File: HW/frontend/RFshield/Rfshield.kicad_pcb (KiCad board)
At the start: 4 copper layers, 73 x 50.9 mm, 139 parts, among them P10 TXENABLE, P11 RXENABLE, P2 VAA, P26 GND, P27 GND, P29 GND, P38 CLKIN, P39 CLKOUT, Q1 MOSFET_P, T1 RX_BALUN, T2 TX_BALUN, U1 MAX2837, U2 MAX5864, U3 SI5351C, X1 GSG-XTAL4PIN

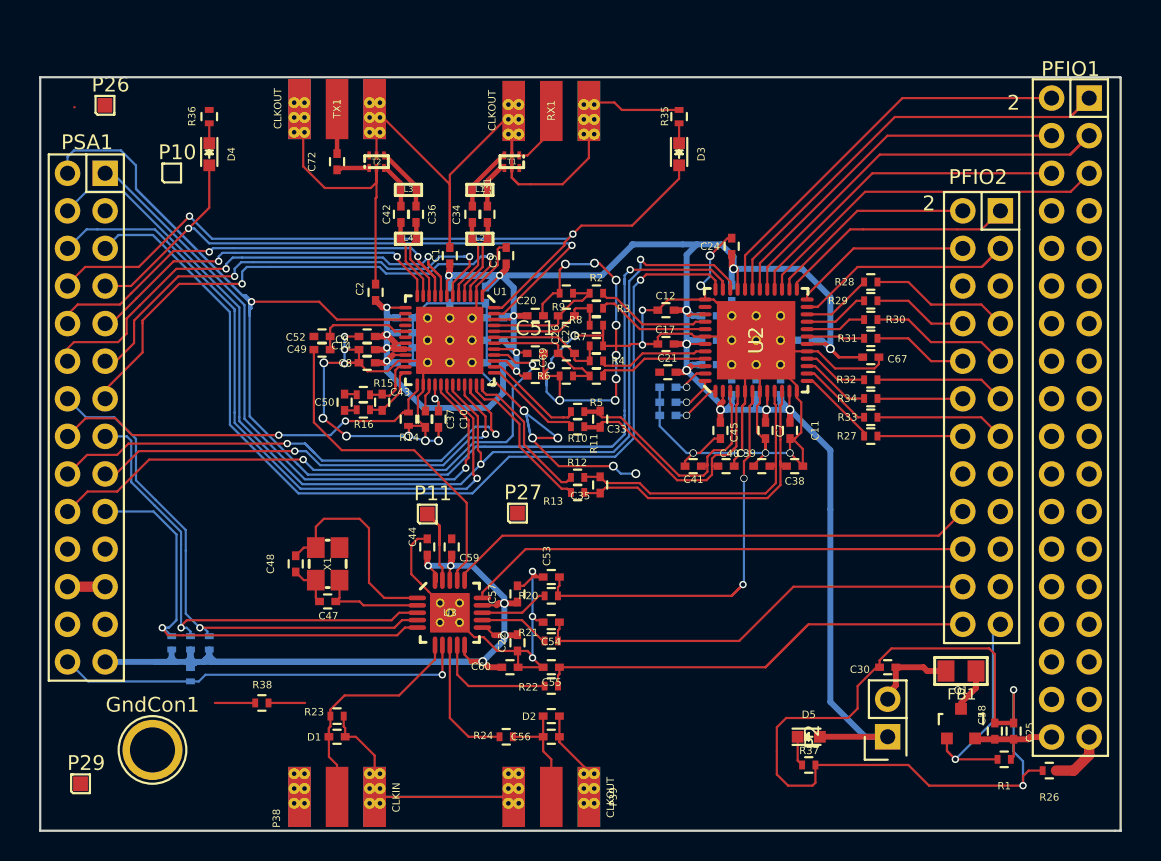
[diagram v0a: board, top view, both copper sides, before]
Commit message: bypass capacitors y planos de tierra agregados
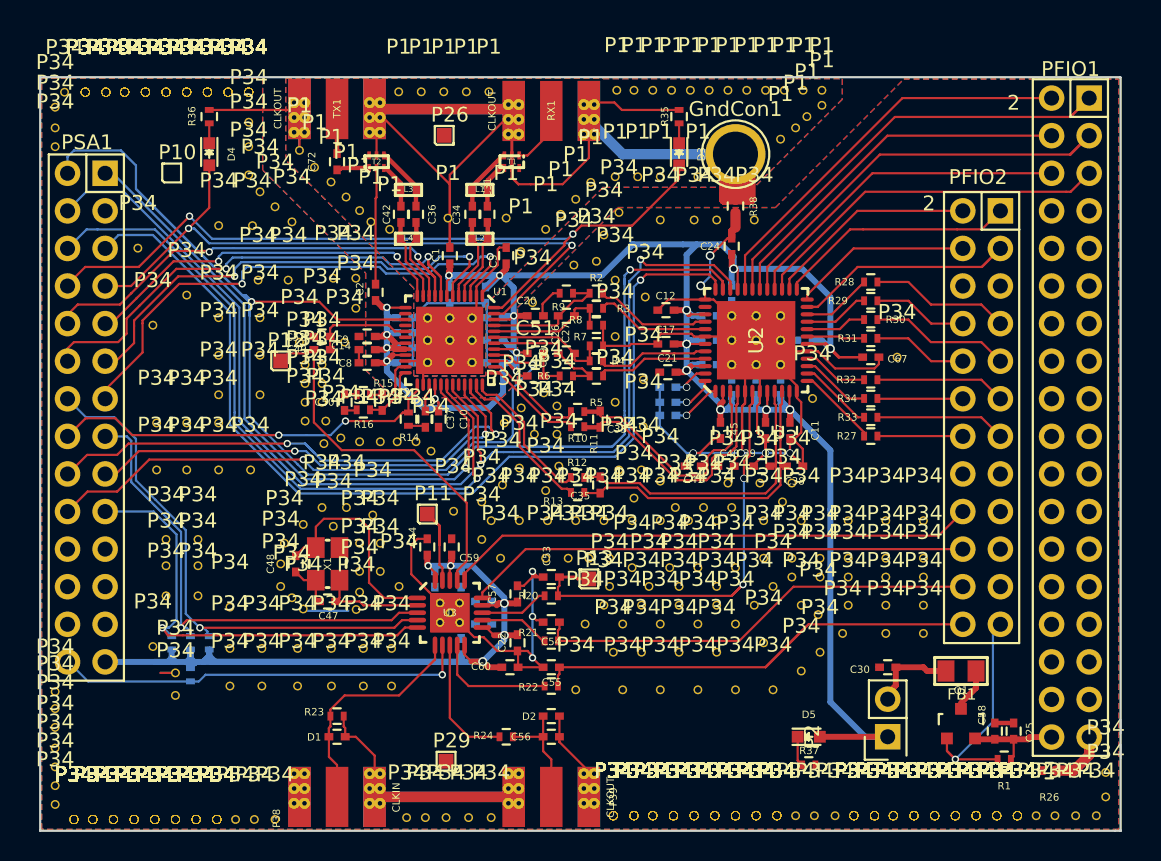
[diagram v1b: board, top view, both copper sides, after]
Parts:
- removed P27: GND, Connect:testpoint1mm
- added C70: 2.2uF, Capacitors_SMD:C_0402, B.Cu at (50.3, 104.1)
- added C71: 2.2uF, Capacitors_SMD:C_0402, B.Cu at (48.8, 105.7)
- added C73: 2.2uF, Capacitors_SMD:C_0402, B.Cu at (50.3, 102.6)
- added C74: 2.2uF, Capacitors_SMD:C_0402, B.Cu at (47.0, 101.1)
- added C75: 2.2uF, Capacitors_SMD:C_0402, B.Cu at (48.8, 101.1)
- added P1: CONN_01X01, Connect:GSG-HOLE-06mm1, F.Cu at (43.9, 77.5)
- added P1: CONN_01X01, Connect:GSG-HOLE-06mm1, F.Cu at (73.2, 69.1)
- added P1: CONN_01X01, Connect:GSG-HOLE-06mm1, F.Cu at (73.2, 68.1)
- added P1: CONN_01X01, Connect:GSG-HOLE-06mm1, F.Cu at (71.9, 68.1)
- added P1: CONN_01X01, Connect:GSG-HOLE-06mm1, F.Cu at (70.6, 68.1)
- added P1: CONN_01X01, Connect:GSG-HOLE-06mm1, F.Cu at (69.3, 68.1)
- added P1: CONN_01X01, Connect:GSG-HOLE-06mm1, F.Cu at (68.1, 68.1)
- added P1: CONN_01X01, Connect:GSG-HOLE-06mm1, F.Cu at (66.8, 68.1)
- added P1: CONN_01X01, Connect:GSG-HOLE-06mm1, F.Cu at (65.5, 68.1)
- added P1: CONN_01X01, Connect:GSG-HOLE-06mm1, F.Cu at (64.3, 68.1)
- added P1: CONN_01X01, Connect:GSG-HOLE-06mm1, F.Cu at (63.0, 68.1)
- added P1: CONN_01X01, Connect:GSG-HOLE-06mm1, F.Cu at (42.7, 77.0)
- added P1: CONN_01X01, Connect:GSG-HOLE-06mm1, F.Cu at (61.7, 68.1)
- added P1: CONN_01X01, Connect:GSG-HOLE-06mm1, F.Cu at (40.0, 74.3)
- added P1: CONN_01X01, Connect:GSG-HOLE-06mm1, F.Cu at (60.5, 68.1)
- added P1: CONN_01X01, Connect:GSG-HOLE-06mm1, F.Cu at (59.3, 68.1)
- added P1: CONN_01X01, Connect:GSG-HOLE-06mm1, F.Cu at (52.8, 79.0)
- added P1: CONN_01X01, Connect:GSG-HOLE-06mm1, F.Cu at (38.9, 73.3)
- added P1: CONN_01X01, Connect:GSG-HOLE-06mm1, F.Cu at (41.0, 75.3)
- added P1: CONN_01X01, Connect:GSG-HOLE-06mm1, F.Cu at (37.8, 72.1)
- added P1: CONN_01X01, Connect:GSG-HOLE-06mm1, F.Cu at (47.9, 76.7)
- added P1: CONN_01X01, Connect:GSG-HOLE-06mm1, F.Cu at (41.9, 76.2)
- added P1: CONN_01X01, Connect:GSG-HOLE-06mm1, F.Cu at (60.7, 73.9)
- added P1: CONN_01X01, Connect:GSG-HOLE-06mm1, F.Cu at (54.5, 77.5)
- added P1: CONN_01X01, Connect:GSG-HOLE-06mm1, F.Cu at (55.5, 76.5)
- added P1: CONN_01X01, Connect:GSG-HOLE-06mm1, F.Cu at (56.5, 75.4)
- added P1: CONN_01X01, Connect:GSG-HOLE-06mm1, F.Cu at (57.5, 74.3)
- added P1: CONN_01X01, Connect:GSG-HOLE-06mm1, F.Cu at (50.6, 68.2)
- added P1: CONN_01X01, Connect:GSG-HOLE-06mm1, F.Cu at (49.1, 68.2)
- added P1: CONN_01X01, Connect:GSG-HOLE-06mm1, F.Cu at (47.6, 68.2)
- added P1: CONN_01X01, Connect:GSG-HOLE-06mm1, F.Cu at (46.1, 68.2)
- added P1: CONN_01X01, Connect:GSG-HOLE-06mm1, F.Cu at (44.6, 68.2)
- added P1: CONN_01X01, Connect:GSG-HOLE-06mm1, F.Cu at (51.8, 76.7)
- added P1: CONN_01X01, Connect:GSG-HOLE-06mm1, F.Cu at (59.2, 73.9)
- added P1: CONN_01X01, Connect:GSG-HOLE-06mm1, F.Cu at (62.2, 73.9)
- added P1: CONN_01X01, Connect:GSG-HOLE-06mm1, F.Cu at (64.8, 73.9)
- added P1: CONN_01X01, Connect:GSG-HOLE-06mm1, F.Cu at (70.4, 71.4)
- added P1: CONN_01X01, Connect:GSG-HOLE-06mm1, F.Cu at (71.4, 70.6)
- added P1: CONN_01X01, Connect:GSG-HOLE-06mm1, F.Cu at (72.1, 69.8)
- added P12: XTAL2, Connect:testpoint1mm, F.Cu at (36.6, 86.4)
- added P13: GCK1, Connect:testpoint1mm, F.Cu at (57.4, 101.1)
- added P34: CONN_01X01, Connect:GSG-HOLE-06mm1, F.Cu at (78.2, 86.1)
- added P34: CONN_01X01, Connect:GSG-HOLE-06mm1, F.Cu at (28.8, 100.2)
- added P34 (x16): CONN_01X01, Connect:GSG-HOLE-06mm1, F.Cu at (24.8, 68.2)
- added P34 (x16): CONN_01X01, Connect:GSG-HOLE-06mm1, F.Cu at (23.4, 68.2)
- added P34 (x16): CONN_01X01, Connect:GSG-HOLE-06mm1, F.Cu at (26.0, 68.2)
- added P34 (x16): CONN_01X01, Connect:GSG-HOLE-06mm1, F.Cu at (27.4, 68.2)
- added P34 (x16): CONN_01X01, Connect:GSG-HOLE-06mm1, F.Cu at (28.8, 68.2)
- added P34 (x16): CONN_01X01, Connect:GSG-HOLE-06mm1, F.Cu at (30.2, 68.2)
- added P34 (x16): CONN_01X01, Connect:GSG-HOLE-06mm1, F.Cu at (31.6, 68.2)
- added P34 (x16): CONN_01X01, Connect:GSG-HOLE-06mm1, F.Cu at (33.0, 68.2)
- added P34: CONN_01X01, Connect:GSG-HOLE-06mm1, F.Cu at (31.0, 98.4)
- added P34 (x16): CONN_01X01, Connect:GSG-HOLE-06mm1, F.Cu at (34.4, 68.2)
- added P34: CONN_01X01, Connect:GSG-HOLE-06mm1, F.Cu at (28.8, 98.4)
- added P34: CONN_01X01, Connect:GSG-HOLE-06mm1, F.Cu at (26.9, 78.7)
- added P34: CONN_01X01, Connect:GSG-HOLE-06mm1, F.Cu at (30.2, 81.9)
- added P34: CONN_01X01, Connect:GSG-HOLE-06mm1, F.Cu at (27.9, 83.9)
- added P34: CONN_01X01, Connect:GSG-HOLE-06mm1, F.Cu at (37.1, 80.9)
- added P34: CONN_01X01, Connect:GSG-HOLE-06mm1, F.Cu at (34.7, 77.2)
- added P34: CONN_01X01, Connect:GSG-HOLE-06mm1, F.Cu at (35.1, 80.9)
- added P34: CONN_01X01, Connect:GSG-HOLE-06mm1, F.Cu at (32.4, 77.2)
- added P34: CONN_01X01, Connect:GSG-HOLE-06mm1, F.Cu at (88.9, 117.1)
- added P34: CONN_01X01, Connect:GSG-HOLE-06mm1, F.Cu at (90.3, 117.1)
- added P34: CONN_01X01, Connect:GSG-HOLE-06mm1, F.Cu at (87.6, 117.1)
- added P34 (x16): CONN_01X01, Connect:GSG-HOLE-06mm1, F.Cu at (75.3, 117.1)
- added P34 (x16): CONN_01X01, Connect:GSG-HOLE-06mm1, F.Cu at (76.7, 117.1)
- added P34 (x16): CONN_01X01, Connect:GSG-HOLE-06mm1, F.Cu at (78.0, 117.1)
- added P34 (x16): CONN_01X01, Connect:GSG-HOLE-06mm1, F.Cu at (79.4, 117.1)
- added P34 (x16): CONN_01X01, Connect:GSG-HOLE-06mm1, F.Cu at (80.8, 117.1)
- added P34: CONN_01X01, Connect:GSG-HOLE-06mm1, F.Cu at (53.6, 82.4)
- added P34: CONN_01X01, Connect:GSG-HOLE-06mm1, F.Cu at (35.2, 88.6)
- added P34 (x16): CONN_01X01, Connect:GSG-HOLE-06mm1, F.Cu at (82.2, 117.1)
- added P34 (x16): CONN_01X01, Connect:GSG-HOLE-06mm1, F.Cu at (83.6, 117.1)
- added P34 (x16): CONN_01X01, Connect:GSG-HOLE-06mm1, F.Cu at (85.0, 117.1)
- added P34 (x16): CONN_01X01, Connect:GSG-HOLE-06mm1, F.Cu at (86.4, 117.1)
- added P34: CONN_01X01, Connect:GSG-HOLE-06mm1, F.Cu at (35.2, 86.0)
- added P34: CONN_01X01, Connect:GSG-HOLE-06mm1, F.Cu at (35.2, 83.4)
- added P34: CONN_01X01, Connect:GSG-HOLE-06mm1, F.Cu at (32.4, 88.6)
- added P34: CONN_01X01, Connect:GSG-HOLE-06mm1, F.Cu at (32.4, 86.0)
- added P34: CONN_01X01, Connect:GSG-HOLE-06mm1, F.Cu at (32.4, 83.4)
- added P34: CONN_01X01, Connect:GSG-HOLE-06mm1, F.Cu at (32.4, 90.6)
- added P34: CONN_01X01, Connect:GSG-HOLE-06mm1, F.Cu at (30.2, 90.6)
- added P34: CONN_01X01, Connect:GSG-HOLE-06mm1, F.Cu at (28.2, 90.6)
- added P34: CONN_01X01, Connect:GSG-HOLE-06mm1, F.Cu at (34.5, 93.7)
- added P34: CONN_01X01, Connect:GSG-HOLE-06mm1, F.Cu at (58.4, 77.9)
- added P34: CONN_01X01, Connect:GSG-HOLE-06mm1, F.Cu at (32.4, 93.7)
- added P34: CONN_01X01, Connect:GSG-HOLE-06mm1, F.Cu at (30.2, 93.7)
- added P34: CONN_01X01, Connect:GSG-HOLE-06mm1, F.Cu at (28.2, 93.7)
- added P34: CONN_01X01, Connect:GSG-HOLE-06mm1, F.Cu at (34.4, 70.2)
- added P34 (x16): CONN_01X01, Connect:GSG-HOLE-06mm1, F.Cu at (59.1, 117.1)
- added P34: CONN_01X01, Connect:GSG-HOLE-06mm1, F.Cu at (34.4, 71.9)
- added P34 (x16): CONN_01X01, Connect:GSG-HOLE-06mm1, F.Cu at (60.5, 117.1)
- added P34 (x16): CONN_01X01, Connect:GSG-HOLE-06mm1, F.Cu at (61.7, 117.1)
- added P34 (x16): CONN_01X01, Connect:GSG-HOLE-06mm1, F.Cu at (63.1, 117.1)
- added P34 (x16): CONN_01X01, Connect:GSG-HOLE-06mm1, F.Cu at (64.5, 117.1)
- added P34 (x16): CONN_01X01, Connect:GSG-HOLE-06mm1, F.Cu at (65.9, 117.1)
- added P34 (x16): CONN_01X01, Connect:GSG-HOLE-06mm1, F.Cu at (67.3, 117.1)
- added P34 (x16): CONN_01X01, Connect:GSG-HOLE-06mm1, F.Cu at (68.7, 117.1)
- added P34 (x16): CONN_01X01, Connect:GSG-HOLE-06mm1, F.Cu at (70.1, 117.1)
- added P34: CONN_01X01, Connect:GSG-HOLE-06mm1, F.Cu at (34.4, 73.8)
- added P34: CONN_01X01, Connect:GSG-HOLE-06mm1, F.Cu at (35.2, 74.9)
- added P34: CONN_01X01, Connect:GSG-HOLE-06mm1, F.Cu at (21.3, 116.3)
- added P34: CONN_01X01, Connect:GSG-HOLE-06mm1, F.Cu at (21.3, 115.1)
- added P34: CONN_01X01, Connect:GSG-HOLE-06mm1, F.Cu at (21.3, 113.8)
- added P34: CONN_01X01, Connect:GSG-HOLE-06mm1, F.Cu at (56.4, 79.9)
- added P34: CONN_01X01, Connect:GSG-HOLE-06mm1, F.Cu at (21.3, 112.5)
- added P34: CONN_01X01, Connect:GSG-HOLE-06mm1, F.Cu at (21.3, 111.1)
- added P34: CONN_01X01, Connect:GSG-HOLE-06mm1, F.Cu at (21.3, 109.9)
- added P34: CONN_01X01, Connect:GSG-HOLE-06mm1, F.Cu at (21.3, 108.7)
- added P34: CONN_01X01, Connect:GSG-HOLE-06mm1, F.Cu at (21.3, 71.9)
- added P34: CONN_01X01, Connect:GSG-HOLE-06mm1, F.Cu at (21.3, 70.6)
- added P34: CONN_01X01, Connect:GSG-HOLE-06mm1, F.Cu at (21.3, 69.2)
- added P34: CONN_01X01, Connect:GSG-HOLE-06mm1, F.Cu at (22.0, 68.2)
- added P34: CONN_01X01, Connect:GSG-HOLE-06mm1, F.Cu at (71.4, 117.1)
- added P34: CONN_01X01, Connect:GSG-HOLE-06mm1, F.Cu at (74.0, 117.1)
- added P34: CONN_01X01, Connect:GSG-HOLE-06mm1, F.Cu at (72.6, 117.1)
- added P34: CONN_01X01, Connect:GSG-HOLE-06mm1, F.Cu at (59.2, 84.7)
- added P34 (x16): CONN_01X01, Connect:GSG-HOLE-06mm1, F.Cu at (22.6, 117.3)
- added P34 (x16): CONN_01X01, Connect:GSG-HOLE-06mm1, F.Cu at (23.9, 117.3)
- added P34 (x16): CONN_01X01, Connect:GSG-HOLE-06mm1, F.Cu at (25.3, 117.3)
- added P34 (x16): CONN_01X01, Connect:GSG-HOLE-06mm1, F.Cu at (26.7, 117.3)
- added P34 (x16): CONN_01X01, Connect:GSG-HOLE-06mm1, F.Cu at (28.1, 117.3)
- added P34 (x16): CONN_01X01, Connect:GSG-HOLE-06mm1, F.Cu at (29.5, 117.3)
- added P34 (x16): CONN_01X01, Connect:GSG-HOLE-06mm1, F.Cu at (30.9, 117.3)
- added P34 (x16): CONN_01X01, Connect:GSG-HOLE-06mm1, F.Cu at (32.3, 117.3)
- added P34: CONN_01X01, Connect:GSG-HOLE-06mm1, F.Cu at (59.2, 80.9)
- added P34: CONN_01X01, Connect:GSG-HOLE-06mm1, F.Cu at (43.3, 100.6)
- added P34: CONN_01X01, Connect:GSG-HOLE-06mm1, F.Cu at (64.5, 76.8)
- added P34: CONN_01X01, Connect:GSG-HOLE-06mm1, F.Cu at (52.7, 93.6)
- added P34: CONN_01X01, Connect:GSG-HOLE-06mm1, F.Cu at (43.3, 98.7)
- added P34: CONN_01X01, Connect:GSG-HOLE-06mm1, F.Cu at (61.1, 87.6)
- added P34: CONN_01X01, Connect:GSG-HOLE-06mm1, F.Cu at (61.2, 82.0)
- added P34: CONN_01X01, Connect:GSG-HOLE-06mm1, F.Cu at (68.6, 76.8)
- added P34: CONN_01X01, Connect:GSG-HOLE-06mm1, F.Cu at (66.0, 76.8)
- added P34: CONN_01X01, Connect:GSG-HOLE-06mm1, F.Cu at (44.6, 101.6)
- added P34: CONN_01X01, Connect:GSG-HOLE-06mm1, F.Cu at (42.8, 96.8)
- added P34: CONN_01X01, Connect:GSG-HOLE-06mm1, F.Cu at (36.6, 101.6)
- added P34: CONN_01X01, Connect:GSG-HOLE-06mm1, F.Cu at (57.9, 79.6)
- added P34: CONN_01X01, Connect:GSG-HOLE-06mm1, F.Cu at (61.1, 90.8)
- added P34: CONN_01X01, Connect:GSG-HOLE-06mm1, F.Cu at (36.6, 100.1)
- added P34: CONN_01X01, Connect:GSG-HOLE-06mm1, F.Cu at (40.1, 80.8)
- added P34: CONN_01X01, Connect:GSG-HOLE-06mm1, F.Cu at (67.3, 108.6)
- added P34: CONN_01X01, Connect:GSG-HOLE-06mm1, F.Cu at (33.5, 117.3)
- added P34: CONN_01X01, Connect:GSG-HOLE-06mm1, F.Cu at (92.3, 115.8)
- added P34: CONN_01X01, Connect:GSG-HOLE-06mm1, F.Cu at (49.3, 117.2)
- added P34: CONN_01X01, Connect:GSG-HOLE-06mm1, F.Cu at (36.2, 117.3)
- added P34: CONN_01X01, Connect:GSG-HOLE-06mm1, F.Cu at (34.8, 117.3)
- added P34: CONN_01X01, Connect:GSG-HOLE-06mm1, F.Cu at (50.8, 117.2)
- added P34: CONN_01X01, Connect:GSG-HOLE-06mm1, F.Cu at (46.4, 117.2)
- added P34: CONN_01X01, Connect:GSG-HOLE-06mm1, F.Cu at (47.8, 117.2)
- added P34: CONN_01X01, Connect:GSG-HOLE-06mm1, F.Cu at (92.3, 114.2)
- added P34: CONN_01X01, Connect:GSG-HOLE-06mm1, F.Cu at (45.1, 117.2)
- added P34: CONN_01X01, Connect:GSG-HOLE-06mm1, F.Cu at (36.2, 75.9)
- added P34: CONN_01X01, Connect:GSG-HOLE-06mm1, F.Cu at (80.0, 102.9)
- added P34: CONN_01X01, Connect:GSG-HOLE-06mm1, F.Cu at (59.4, 93.7)
- added P34: CONN_01X01, Connect:GSG-HOLE-06mm1, F.Cu at (65.2, 96.3)
- added P34: CONN_01X01, Connect:GSG-HOLE-06mm1, F.Cu at (62.2, 94.5)
- added P34: CONN_01X01, Connect:GSG-HOLE-06mm1, F.Cu at (37.7, 105.8)
- added P34: CONN_01X01, Connect:GSG-HOLE-06mm1, F.Cu at (36.8, 98.7)
- added P34: CONN_01X01, Connect:GSG-HOLE-06mm1, F.Cu at (80.0, 101.0)
- added P34: CONN_01X01, Connect:GSG-HOLE-06mm1, F.Cu at (77.5, 102.9)
- added P34: CONN_01X01, Connect:GSG-HOLE-06mm1, F.Cu at (59.2, 89.2)
- added P34: CONN_01X01, Connect:GSG-HOLE-06mm1, F.Cu at (77.5, 101.0)
- added P34: CONN_01X01, Connect:GSG-HOLE-06mm1, F.Cu at (72.5, 88.9)
- added P34: CONN_01X01, Connect:GSG-HOLE-06mm1, F.Cu at (74.9, 101.0)
- added P34: CONN_01X01, Connect:GSG-HOLE-06mm1, F.Cu at (91.7, 117.1)
- added P34: CONN_01X01, Connect:GSG-HOLE-06mm1, F.Cu at (80.0, 104.8)
- added P34: CONN_01X01, Connect:GSG-HOLE-06mm1, F.Cu at (42.2, 105.8)
- added P34: CONN_01X01, Connect:GSG-HOLE-06mm1, F.Cu at (77.5, 104.8)
- added P34: CONN_01X01, Connect:GSG-HOLE-06mm1, F.Cu at (42.2, 108.3)
- added P34: CONN_01X01, Connect:GSG-HOLE-06mm1, F.Cu at (54.5, 95.1)
- added P34: CONN_01X01, Connect:GSG-HOLE-06mm1, F.Cu at (74.5, 104.8)
- added P34: CONN_01X01, Connect:GSG-HOLE-06mm1, F.Cu at (55.4, 93.5)
- added P34: CONN_01X01, Connect:GSG-HOLE-06mm1, F.Cu at (40.0, 105.8)
- added P34: CONN_01X01, Connect:GSG-HOLE-06mm1, F.Cu at (60.5, 95.6)
- added P34: CONN_01X01, Connect:GSG-HOLE-06mm1, F.Cu at (61.0, 93.7)
- added P34: CONN_01X01, Connect:GSG-HOLE-06mm1, F.Cu at (33.1, 103.0)
- added P34: CONN_01X01, Connect:GSG-HOLE-06mm1, F.Cu at (40.0, 108.3)
- added P34: CONN_01X01, Connect:GSG-HOLE-06mm1, F.Cu at (63.2, 96.3)
- added P34: CONN_01X01, Connect:GSG-HOLE-06mm1, F.Cu at (73.0, 106.0)
- added P34: CONN_01X01, Connect:GSG-HOLE-06mm1, F.Cu at (71.8, 107.3)
- added P34: CONN_01X01, Connect:GSG-HOLE-06mm1, F.Cu at (69.8, 108.6)
- added P34: CONN_01X01, Connect:GSG-HOLE-06mm1, F.Cu at (72.9, 103.5)
- added P34: CONN_01X01, Connect:GSG-HOLE-06mm1, F.Cu at (64.8, 108.6)
- added P34: CONN_01X01, Connect:GSG-HOLE-06mm1, F.Cu at (59.7, 108.6)
- added P34: CONN_01X01, Connect:GSG-HOLE-06mm1, F.Cu at (59.4, 76.3)
- added P34: CONN_01X01, Connect:GSG-HOLE-06mm1, F.Cu at (41.0, 96.3)
- added P34: CONN_01X01, Connect:GSG-HOLE-06mm1, F.Cu at (56.5, 108.6)
- added P34: CONN_01X01, Connect:GSG-HOLE-06mm1, F.Cu at (62.2, 108.6)
- added P34: CONN_01X01, Connect:GSG-HOLE-06mm1, F.Cu at (52.8, 89.5)
- added P34: CONN_01X01, Connect:GSG-HOLE-06mm1, F.Cu at (39.4, 96.3)
- added P34: CONN_01X01, Connect:GSG-HOLE-06mm1, F.Cu at (33.1, 108.3)
- added P34: CONN_01X01, Connect:GSG-HOLE-06mm1, F.Cu at (33.1, 105.8)
- added P34: CONN_01X01, Connect:GSG-HOLE-06mm1, F.Cu at (44.1, 108.3)
- added P34: CONN_01X01, Connect:GSG-HOLE-06mm1, F.Cu at (44.1, 105.8)
- added P34: CONN_01X01, Connect:GSG-HOLE-06mm1, F.Cu at (62.2, 76.8)
- added P34: CONN_01X01, Connect:GSG-HOLE-06mm1, F.Cu at (29.5, 109.0)
- added P34: CONN_01X01, Connect:GSG-HOLE-06mm1, F.Cu at (27.9, 105.7)
- added P34: CONN_01X01, Connect:GSG-HOLE-06mm1, F.Cu at (71.8, 102.9)
- added P34: CONN_01X01, Connect:GSG-HOLE-06mm1, F.Cu at (73.0, 101.0)
- added P34: CONN_01X01, Connect:GSG-HOLE-06mm1, F.Cu at (71.1, 101.0)
- added P34: CONN_01X01, Connect:GSG-HOLE-06mm1, F.Cu at (69.0, 94.6)
- added P34: CONN_01X01, Connect:GSG-HOLE-06mm1, F.Cu at (66.0, 106.0)
- added P34: CONN_01X01, Connect:GSG-HOLE-06mm1, F.Cu at (68.6, 102.9)
- added P34: CONN_01X01, Connect:GSG-HOLE-06mm1, F.Cu at (67.3, 104.1)
- added P34: CONN_01X01, Connect:GSG-HOLE-06mm1, F.Cu at (41.9, 102.0)
- added P34: CONN_01X01, Connect:GSG-HOLE-06mm1, F.Cu at (64.8, 104.1)
- added P34: CONN_01X01, Connect:GSG-HOLE-06mm1, F.Cu at (66.0, 102.9)
- added P34: CONN_01X01, Connect:GSG-HOLE-06mm1, F.Cu at (62.2, 104.1)
- added P34: CONN_01X01, Connect:GSG-HOLE-06mm1, F.Cu at (61.0, 106.0)
- added P34: CONN_01X01, Connect:GSG-HOLE-06mm1, F.Cu at (59.7, 104.1)
- added P34: CONN_01X01, Connect:GSG-HOLE-06mm1, F.Cu at (57.1, 104.1)
- added P34: CONN_01X01, Connect:GSG-HOLE-06mm1, F.Cu at (28.8, 102.2)
- added P34: CONN_01X01, Connect:GSG-HOLE-06mm1, F.Cu at (69.8, 101.6)
- added P34: CONN_01X01, Connect:GSG-HOLE-06mm1, F.Cu at (41.9, 98.7)
- added P34: CONN_01X01, Connect:GSG-HOLE-06mm1, F.Cu at (35.3, 105.8)
- added P34: CONN_01X01, Connect:GSG-HOLE-06mm1, F.Cu at (63.5, 106.0)
- added P34: CONN_01X01, Connect:GSG-HOLE-06mm1, F.Cu at (35.3, 108.3)
- added P34: CONN_01X01, Connect:GSG-HOLE-06mm1, F.Cu at (61.0, 102.9)
- added P34: CONN_01X01, Connect:GSG-HOLE-06mm1, F.Cu at (63.5, 102.9)
- added P34: CONN_01X01, Connect:GSG-HOLE-06mm1, F.Cu at (58.4, 102.9)
- added P34: CONN_01X01, Connect:GSG-HOLE-06mm1, F.Cu at (37.7, 108.3)
- added P34: CONN_01X01, Connect:GSG-HOLE-06mm1, F.Cu at (66.0, 101.6)
- added P34: CONN_01X01, Connect:GSG-HOLE-06mm1, F.Cu at (69.2, 105.4)
- added P34: CONN_01X01, Connect:GSG-HOLE-06mm1, F.Cu at (63.5, 101.6)
- added P34: CONN_01X01, Connect:GSG-HOLE-06mm1, F.Cu at (61.5, 101.6)
- added P34: CONN_01X01, Connect:GSG-HOLE-06mm1, F.Cu at (38.1, 97.4)
- added P34: CONN_01X01, Connect:GSG-HOLE-06mm1, F.Cu at (58.8, 101.6)
- added P34: CONN_01X01, Connect:GSG-HOLE-06mm1, F.Cu at (59.1, 106.0)
- added P34: CONN_01X01, Connect:GSG-HOLE-06mm1, F.Cu at (80.0, 97.2)
- added P34: CONN_01X01, Connect:GSG-HOLE-06mm1, F.Cu at (51.6, 94.7)
- added P34: CONN_01X01, Connect:GSG-HOLE-06mm1, F.Cu at (77.5, 97.2)
- added P34: CONN_01X01, Connect:GSG-HOLE-06mm1, F.Cu at (70.5, 95.9)
- added P34: CONN_01X01, Connect:GSG-HOLE-06mm1, F.Cu at (66.8, 94.6)
- added P34: CONN_01X01, Connect:GSG-HOLE-06mm1, F.Cu at (80.0, 99.7)
- added P34: CONN_01X01, Connect:GSG-HOLE-06mm1, F.Cu at (55.2, 91.3)
- added P34: CONN_01X01, Connect:GSG-HOLE-06mm1, F.Cu at (55.2, 89.4)
- added P34: CONN_01X01, Connect:GSG-HOLE-06mm1, F.Cu at (77.5, 99.7)
- added P34: CONN_01X01, Connect:GSG-HOLE-06mm1, F.Cu at (74.9, 102.9)
- added P34: CONN_01X01, Connect:GSG-HOLE-06mm1, F.Cu at (74.9, 99.7)
- added P34: CONN_01X01, Connect:GSG-HOLE-06mm1, F.Cu at (74.9, 97.2)
- added P34: CONN_01X01, Connect:GSG-HOLE-06mm1, F.Cu at (40.1, 97.5)
- added P34: CONN_01X01, Connect:GSG-HOLE-06mm1, F.Cu at (67.1, 96.3)
- added P34: CONN_01X01, Connect:GSG-HOLE-06mm1, F.Cu at (71.8, 97.2)
- added P34: CONN_01X01, Connect:GSG-HOLE-06mm1, F.Cu at (69.2, 97.2)
- added P34: CONN_01X01, Connect:GSG-HOLE-06mm1, F.Cu at (41.9, 100.6)
- added P34: CONN_01X01, Connect:GSG-HOLE-06mm1, F.Cu at (41.7, 103.2)
- added P34: CONN_01X01, Connect:GSG-HOLE-06mm1, F.Cu at (54.4, 88.5)
- added P34: CONN_01X01, Connect:GSG-HOLE-06mm1, F.Cu at (66.0, 97.2)
- added P34: CONN_01X01, Connect:GSG-HOLE-06mm1, F.Cu at (64.1, 97.2)
- added P34: CONN_01X01, Connect:GSG-HOLE-06mm1, F.Cu at (62.2, 97.2)
- added P34: CONN_01X01, Connect:GSG-HOLE-06mm1, F.Cu at (60.3, 97.2)
- added P34: CONN_01X01, Connect:GSG-HOLE-06mm1, F.Cu at (58.4, 97.2)
- added P34: CONN_01X01, Connect:GSG-HOLE-06mm1, F.Cu at (56.5, 97.2)
- added P34: CONN_01X01, Connect:GSG-HOLE-06mm1, F.Cu at (54.6, 97.2)
- added P34: CONN_01X01, Connect:GSG-HOLE-06mm1, F.Cu at (52.7, 97.2)
- added P34: CONN_01X01, Connect:GSG-HOLE-06mm1, F.Cu at (71.1, 99.7)
- added P34: CONN_01X01, Connect:GSG-HOLE-06mm1, F.Cu at (73.0, 99.7)
- added P34: CONN_01X01, Connect:GSG-HOLE-06mm1, F.Cu at (29.5, 107.4)
- added P34: CONN_01X01, Connect:GSG-HOLE-06mm1, F.Cu at (69.2, 99.7)
- added P34: CONN_01X01, Connect:GSG-HOLE-06mm1, F.Cu at (67.3, 100.3)
- added P34: CONN_01X01, Connect:GSG-HOLE-06mm1, F.Cu at (64.8, 100.3)
- added P34: CONN_01X01, Connect:GSG-HOLE-06mm1, F.Cu at (62.9, 100.3)
- added P34: CONN_01X01, Connect:GSG-HOLE-06mm1, F.Cu at (71.1, 94.6)
- added P34: CONN_01X01, Connect:GSG-HOLE-06mm1, F.Cu at (60.3, 100.3)
- added P34: CONN_01X01, Connect:GSG-HOLE-06mm1, F.Cu at (38.1, 103.1)
- added P34: CONN_01X01, Connect:GSG-HOLE-06mm1, F.Cu at (58.8, 99.7)
- added P34: CONN_01X01, Connect:GSG-HOLE-06mm1, F.Cu at (57.4, 99.7)
- added P34: CONN_01X01, Connect:GSG-HOLE-06mm1, F.Cu at (56.0, 99.7)
- added P34: CONN_01X01, Connect:GSG-HOLE-06mm1, F.Cu at (54.5, 99.7)
- added P34: CONN_01X01, Connect:GSG-HOLE-06mm1, F.Cu at (51.4, 99.7)
- added P34: CONN_01X01, Connect:GSG-HOLE-06mm1, F.Cu at (50.8, 97.2)
- added P34: CONN_01X01, Connect:GSG-HOLE-06mm1, F.Cu at (53.7, 91.3)
- added P34: CONN_01X01, Connect:GSG-HOLE-06mm1, F.Cu at (50.2, 98.4)
- added P34: CONN_01X01, Connect:GSG-HOLE-06mm1, F.Cu at (51.7, 90.6)
- added P34: CONN_01X01, Connect:GSG-HOLE-06mm1, F.Cu at (50.2, 95.9)
- added P34: CONN_01X01, Connect:GSG-HOLE-06mm1, F.Cu at (37.3, 102.4)
- added P34: CONN_01X01, Connect:GSG-HOLE-06mm1, F.Cu at (48.3, 96.5)
- added P34: CONN_01X01, Connect:GSG-HOLE-06mm1, F.Cu at (46.7, 92.5)
- added P34: CONN_01X01, Connect:GSG-HOLE-06mm1, F.Cu at (45.7, 91.8)
- added P34: CONN_01X01, Connect:GSG-HOLE-06mm1, F.Cu at (44.5, 91.8)
- added P34: CONN_01X01, Connect:GSG-HOLE-06mm1, F.Cu at (43.3, 91.8)
- added P34: CONN_01X01, Connect:GSG-HOLE-06mm1, F.Cu at (41.9, 91.8)
- added P34: CONN_01X01, Connect:GSG-HOLE-06mm1, F.Cu at (40.6, 91.6)
- added P34: CONN_01X01, Connect:GSG-HOLE-06mm1, F.Cu at (39.5, 91.9)
- added P34: CONN_01X01, Connect:GSG-HOLE-06mm1, F.Cu at (39.6, 90.4)
- added P34: CONN_01X01, Connect:GSG-HOLE-06mm1, F.Cu at (39.4, 89.2)
- added P34: CONN_01X01, Connect:GSG-HOLE-06mm1, F.Cu at (39.4, 87.9)
- added P34: CONN_01X01, Connect:GSG-HOLE-06mm1, F.Cu at (39.4, 86.6)
- added P34: CONN_01X01, Connect:GSG-HOLE-06mm1, F.Cu at (38.2, 90.4)
- added P34: CONN_01X01, Connect:GSG-HOLE-06mm1, F.Cu at (38.2, 89.2)
- added P34: CONN_01X01, Connect:GSG-HOLE-06mm1, F.Cu at (38.2, 87.9)
- added P34: CONN_01X01, Connect:GSG-HOLE-06mm1, F.Cu at (38.2, 86.6)
- added P34: CONN_01X01, Connect:GSG-HOLE-06mm1, F.Cu at (37.8, 85.1)
- added P34: CONN_01X01, Connect:GSG-HOLE-06mm1, F.Cu at (39.4, 83.7)
- added P34: CONN_01X01, Connect:GSG-HOLE-06mm1, F.Cu at (40.9, 85.1)
- added P34: CONN_01X01, Connect:GSG-HOLE-06mm1, F.Cu at (41.7, 82.8)
- added P34: CONN_01X01, Connect:GSG-HOLE-06mm1, F.Cu at (41.7, 80.8)
- added P34: CONN_01X01, Connect:GSG-HOLE-06mm1, F.Cu at (37.3, 77.0)
- added P34: CONN_01X01, Connect:GSG-HOLE-06mm1, F.Cu at (31.0, 102.2)
- added P34: CONN_01X01, Connect:GSG-HOLE-06mm1, F.Cu at (31.0, 100.2)
- moved GndCon1 56.3 mm to (67.3, 72.4)
- moved R38 46.4 mm to (67.3, 75.9), turned to 270 degrees
- moved P29 24.7 mm to (47.8, 113.4)
- moved P26 23.0 mm to (47.6, 71.1)
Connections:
- C10 pad 2: GND -> 0V_dig
- C14 pad 2: GND -> 0V_dig
- C20 pad 1: VAA -> (no net)
- C20 pad 2: GND -> (no net)
- C25 pad 2: GND -> 0V_dig
- C30 pad 2: GND -> 0V_dig
- C37 pad 2: GND -> 0V_dig
- C51 pad 2: GND -> 0V_dig
- C52 pad 2: GND -> 0V_dig
- C58 pad 2: GND -> 0V_dig
- C69 pad 2: GND -> 0V_dig
- C8 pad 2: GND -> 0V_dig
- C9 pad 2: GND -> 0V_dig
- PSA1 pad 23: GND -> 0V_dig
- PSA1 pad 24: GND -> 0V_dig
- R14 pad 1: GND -> 0V_dig
- R26 pad 2: GND -> 0V_dig
- R37 pad 2: GND -> 0V_dig
- R6 pad 2: GND -> 0V_dig
- R7 pad 2: GND -> 0V_dig
- R8 pad 2: GND -> 0V_dig
- R9 pad 2: GND -> 0V_dig
- U1 pad 16: (no net) -> /XCVR_CLKOUT
- U1 pad 32: (no net) -> RSSI
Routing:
- net GND: track 252.0 -> 148.1 mm, vias 27 -> 0
- net 0V_dig: track 172.5 -> 186.3 mm, vias 11 -> 9
- net /CLK5: track 23.0 -> 25.5 mm
- net GCK1: track 29.3 -> 31.4 mm
- added copper zone on B.Cu, net 0V_dig
- added copper zone on F.Cu, net 0V_dig
- added copper zone on B.Cu, net GND
- added copper zone on F.Cu, net GND

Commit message: revisión 1.0
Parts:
- moved P34 0.51 mm to (54.0, 82.2)
- moved P34 0.50 mm to (74.9, 105.1)
- moved P34 0.38 mm to (80.0, 105.2)
- moved P34 0.37 mm to (55.6, 93.2)
- moved P34 0.32 mm to (32.3, 94.0)
- moved P34 0.32 mm to (34.5, 94.0)
- moved P34 0.32 mm to (30.2, 94.0)
- moved P34 0.32 mm to (28.2, 94.0)
- moved P34 0.32 mm to (59.5, 84.7)
- moved P34 0.32 mm to (77.5, 105.1)
- moved P34 0.32 mm to (55.2, 91.6)
- moved P34 0.26 mm to (32.4, 90.3)
- moved P34 0.26 mm to (35.4, 108.1)
- moved P34 0.26 mm to (30.3, 90.3)
- moved P34 0.26 mm to (28.3, 90.3)
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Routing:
- net VAA: track 188.7 -> 181.1 mm
- net 0V_dig: track 186.3 -> 192.6 mm
- net VCC: track 76.1 -> 80.3 mm

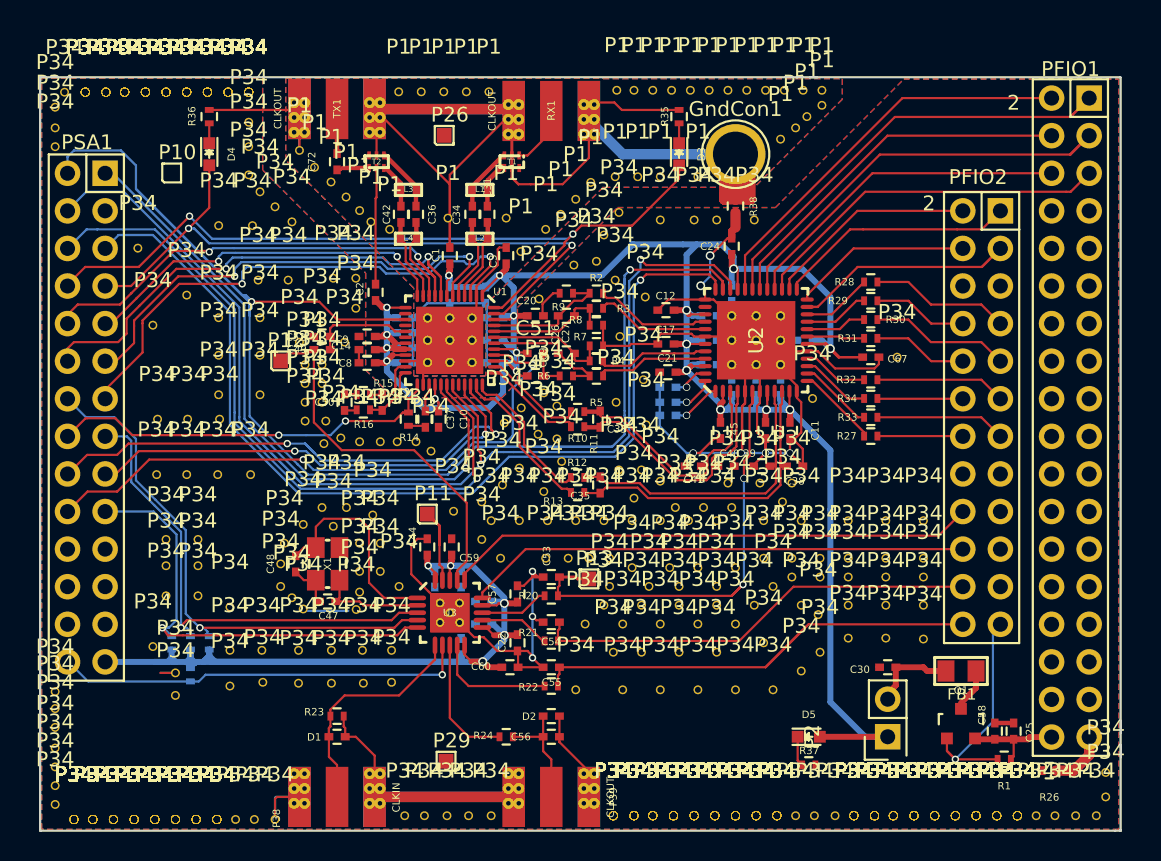
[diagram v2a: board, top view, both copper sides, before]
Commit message: text sixe and ground plane fixed,
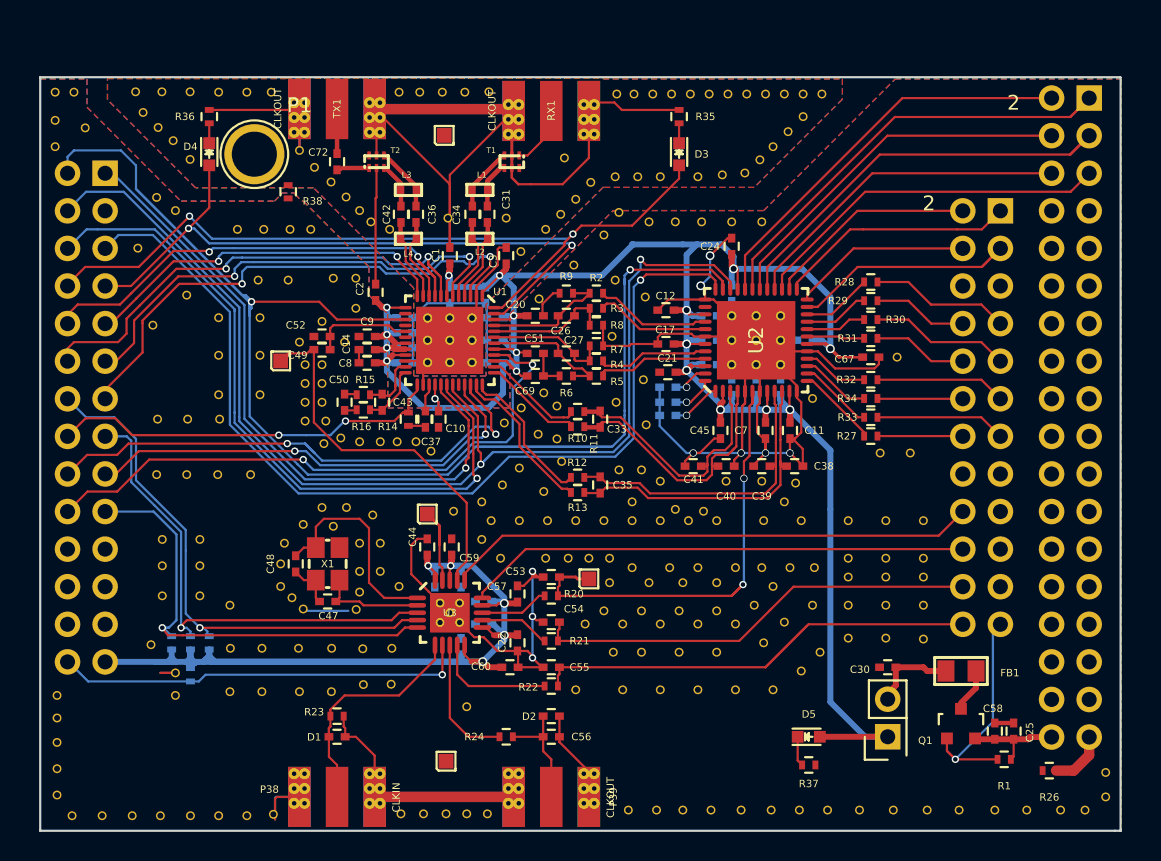
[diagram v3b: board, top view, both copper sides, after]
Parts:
- removed the P1 at (43.9, 77.5)
- removed the P1 at (42.7, 77.0)
- removed the P1 at (60.7, 73.9)
- removed P10: TXENABLE, Connect:testpoint1mm
- removed P34 (x572): CONN_01X01, Connect:GSG-HOLE-06mm1
- added ?: CONN_01X01, Connect:GSG-HOLE-06mm1, F.Cu at (49.0, 68.2)
- added ?: CONN_01X01, Connect:GSG-HOLE-06mm1, F.Cu at (66.4, 73.8)
- added ?: CONN_01X01, Connect:GSG-HOLE-06mm1, F.Cu at (30.5, 72.7)
- added ?: CONN_01X01, Connect:GSG-HOLE-06mm1, F.Cu at (29.3, 71.5)
- added ?: CONN_01X01, Connect:GSG-HOLE-06mm1, F.Cu at (28.3, 70.6)
- added ?: CONN_01X01, Connect:GSG-HOLE-06mm1, F.Cu at (27.3, 69.6)
- added ?: CONN_01X01, Connect:GSG-HOLE-06mm1, F.Cu at (26.8, 68.2)
- added ?: CONN_01X01, Connect:GSG-HOLE-06mm1, F.Cu at (28.5, 68.2)
- added ?: CONN_01X01, Connect:GSG-HOLE-06mm1, F.Cu at (30.5, 68.2)
- added ?: CONN_01X01, Connect:GSG-HOLE-06mm1, F.Cu at (44.6, 68.2)
- added ?: CONN_01X01, Connect:GSG-HOLE-06mm1, F.Cu at (46.0, 68.2)
- added ?: CONN_01X01, Connect:GSG-HOLE-06mm1, F.Cu at (28.2, 75.3)
- added ?: CONN_01X01, Connect:GSG-HOLE-06mm1, F.Cu at (87.0, 116.7)
- added ?: CONN_01X01, Connect:GSG-HOLE-06mm1, F.Cu at (84.8, 116.7)
- added ?: CONN_01X01, Connect:GSG-HOLE-06mm1, F.Cu at (82.4, 116.7)
- added ?: CONN_01X01, Connect:GSG-HOLE-06mm1, F.Cu at (80.3, 116.7)
- added ?: CONN_01X01, Connect:GSG-HOLE-06mm1, F.Cu at (78.0, 116.7)
- added ?: CONN_01X01, Connect:GSG-HOLE-06mm1, F.Cu at (75.7, 116.7)
- added ?: CONN_01X01, Connect:GSG-HOLE-06mm1, F.Cu at (73.5, 116.7)
- added ?: CONN_01X01, Connect:GSG-HOLE-06mm1, F.Cu at (71.6, 116.7)
- added ?: CONN_01X01, Connect:GSG-HOLE-06mm1, F.Cu at (69.7, 116.7)
- added ?: CONN_01X01, Connect:GSG-HOLE-06mm_nt, F.Cu at (43.9, 77.5)
- added ?: CONN_01X01, Connect:GSG-HOLE-06mm_nt, F.Cu at (78.2, 86.1)
- added ?: CONN_01X01, Connect:GSG-HOLE-06mm1, F.Cu at (67.7, 116.7)
- added ?: CONN_01X01, Connect:GSG-HOLE-06mm_nt, F.Cu at (42.7, 77.0)
- added ?: CONN_01X01, Connect:GSG-HOLE-06mm_nt, F.Cu at (54.0, 82.2)
- added ?: CONN_01X01, Connect:GSG-HOLE-06mm_nt, F.Cu at (60.7, 73.9)
- added ?: CONN_01X01, Connect:GSG-HOLE-06mm_nt, F.Cu at (58.4, 77.9)
- added ?: CONN_01X01, Connect:GSG-HOLE-06mm1, F.Cu at (29.5, 76.2)
- added ?: CONN_01X01, Connect:GSG-HOLE-06mm1, F.Cu at (65.7, 116.7)
- added ?: CONN_01X01, Connect:GSG-HOLE-06mm1, F.Cu at (63.8, 116.7)
- added ?: CONN_01X01, Connect:GSG-HOLE-06mm1, F.Cu at (62.0, 116.7)
- added ?: CONN_01X01, Connect:GSG-HOLE-06mm1, F.Cu at (60.1, 116.7)
- added ?: CONN_01X01, Connect:GSG-HOLE-06mm1, F.Cu at (23.4, 70.6)
- added ?: CONN_01X01, Connect:GSG-HOLE-06mm1, F.Cu at (49.1, 109.7)
- added ?: CONN_01X01, Connect:GSG-HOLE-06mm1, F.Cu at (22.6, 68.2)
- added ?: CONN_01X01, Connect:GSG-HOLE-06mm1, F.Cu at (21.3, 68.2)
- added ?: CONN_01X01, Connect:GSG-HOLE-06mm1, F.Cu at (55.8, 72.6)
- added ?: CONN_01X01, Connect:GSG-HOLE-06mm1, F.Cu at (71.9, 69.8)
- ?: renamed from P34; footprint Connect:GSG-HOLE-06mm1 -> Connect:GSG-HOLE-06mm_nt
- PFIO1: footprint Socket_Strips:Socket_Strip_Straight_2x18 -> Socket_Strips:Socket_Strip_Straight_2x18_B
- PFIO2: footprint Socket_Strips:Socket_Strip_Straight_2x12 -> Socket_Strips:Socket_Strip_Straight_2x12_B
- PSA1: footprint Socket_Strips:Socket_Strip_Straight_2x14 -> Socket_Strips:Socket_Strip_Straight_2x14_B
- moved ? 32.5 mm to (34.8, 72.4)
- moved R38 30.2 mm to (37.1, 74.9)
- moved ? 15.2 mm to (32.4, 68.2)
- moved ? 11.8 mm to (34.3, 68.2)
- moved ? 11.7 mm to (34.3, 117.1)
- moved ? 9.78 mm to (32.4, 117.1)
- moved ? 9.37 mm to (79.1, 92.6)
- moved ? 9.28 mm to (77.1, 92.6)
- moved ? 8.61 mm to (35.9, 68.2)
- moved ? 7.88 mm to (30.5, 117.1)
- moved ? 6.10 mm to (21.5, 109.0)
- moved ? 6.08 mm to (22.5, 117.1)
- moved ? 5.85 mm to (28.4, 117.1)
- moved ? 5.84 mm to (21.5, 115.7)
- moved ? 4.45 mm to (61.5, 77.0)
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- renumbered P34 to ?, P1 to ?, P11 to ?, P26 to ?, P29 to ?, GndCon1 to ?, P2 to ?, P12 to ?, P13 to ?
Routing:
- net GND: track 148.1 -> 118.8 mm
- net 0V_dig: track 192.6 -> 190.7 mm

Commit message: revisión 2.0
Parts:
- moved P1 0.76 mm to (37.8, 72.9)
- moved ? 0.74 mm to (38.5, 73.9)
- moved ? 0.64 mm to (30.9, 81.9)
- moved ? 0.64 mm to (36.6, 87.0)
- moved ? 0.57 mm to (27.4, 78.5)
- moved ? 0.46 mm to (72.6, 105.9)
- moved ? 0.41 mm to (40.0, 74.7)
- moved ? 0.40 mm to (43.6, 77.3)
- moved ? 0.30 mm to (40.9, 75.6)
- moved ? 0.28 mm to (42.4, 77.1)
- moved ? 0.28 mm to (41.7, 76.3)
- moved ? 0.25 mm to (67.9, 73.9)
- moved ? 0.18 mm to (61.8, 68.2)
- moved ? 0.13 mm to (72.6, 102.9)
- moved ? 0.13 mm to (66.4, 73.9)
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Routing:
- net GND: track 118.8 -> 165.0 mm
- net 0V_dig: track 190.7 -> 194.3 mm
- net !VAA_ENABLE: track 15.7 -> 16.4 mm
- net /CLK5: track 25.5 -> 26.2 mm
